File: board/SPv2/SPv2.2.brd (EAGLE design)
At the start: 60 x 22.9 mm, 35 parts, among them IC1 S34ML0XG1, IC2 F5508, IC4 74LS14D, Q1 12MHz

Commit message: * some updates for v2.2 of the board (reducing components) * cleaning up error code * verifying R codes do work
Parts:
- moved D1 2.25 mm to (13.3, 6.35)
- moved R21 0.32 mm to (19.5, 10.8)
- flipped SJ1 to the bottom, turned to 0 degrees
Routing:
- net GND: track 169.0 -> 164.6 mm, vias 9 -> 8
- net VBUS: track 87.8 -> 84.5 mm
- net N$4: track 2.86 -> 0.02 mm
- net PUR_A: track 15.0 -> 12.5 mm
- net N$33: track 4.52 -> 6.59 mm

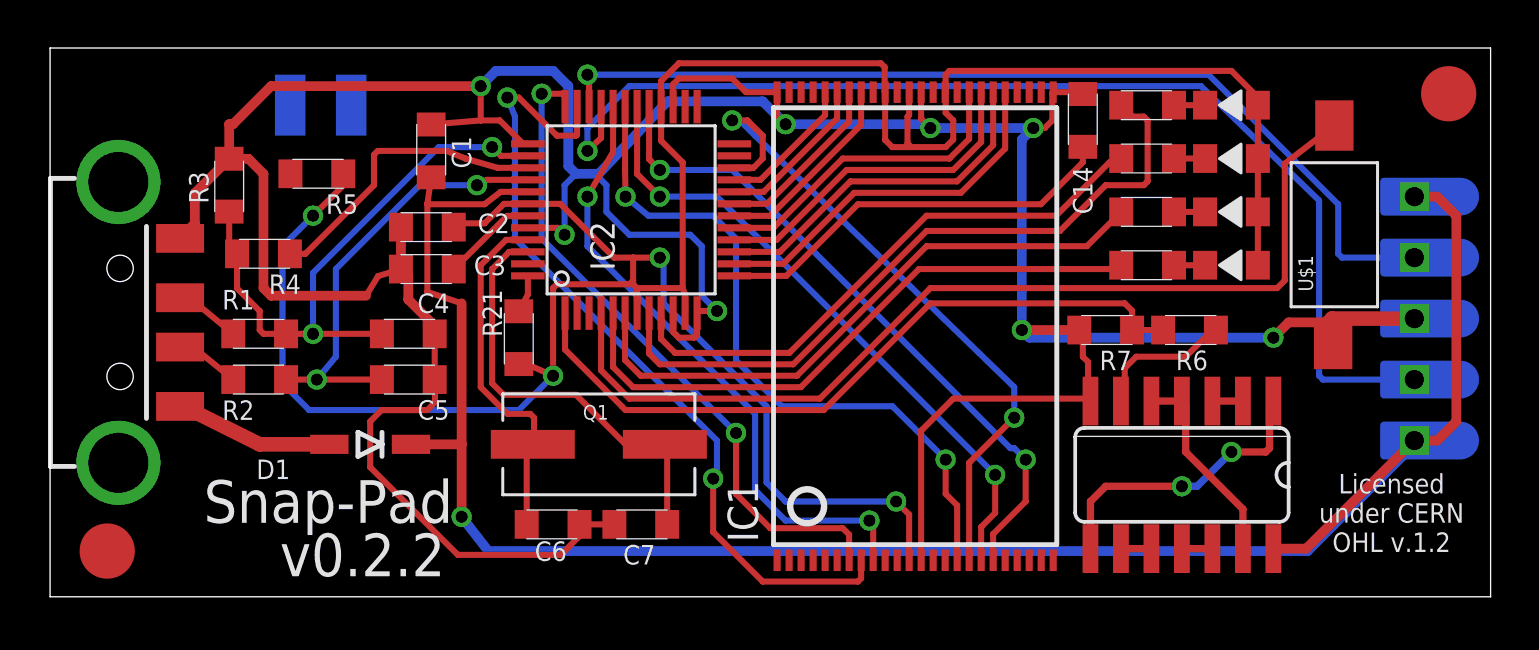
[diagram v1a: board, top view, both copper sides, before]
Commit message: new switch smaller 74ls14 jumper header instead of solder jumper board layout in progress
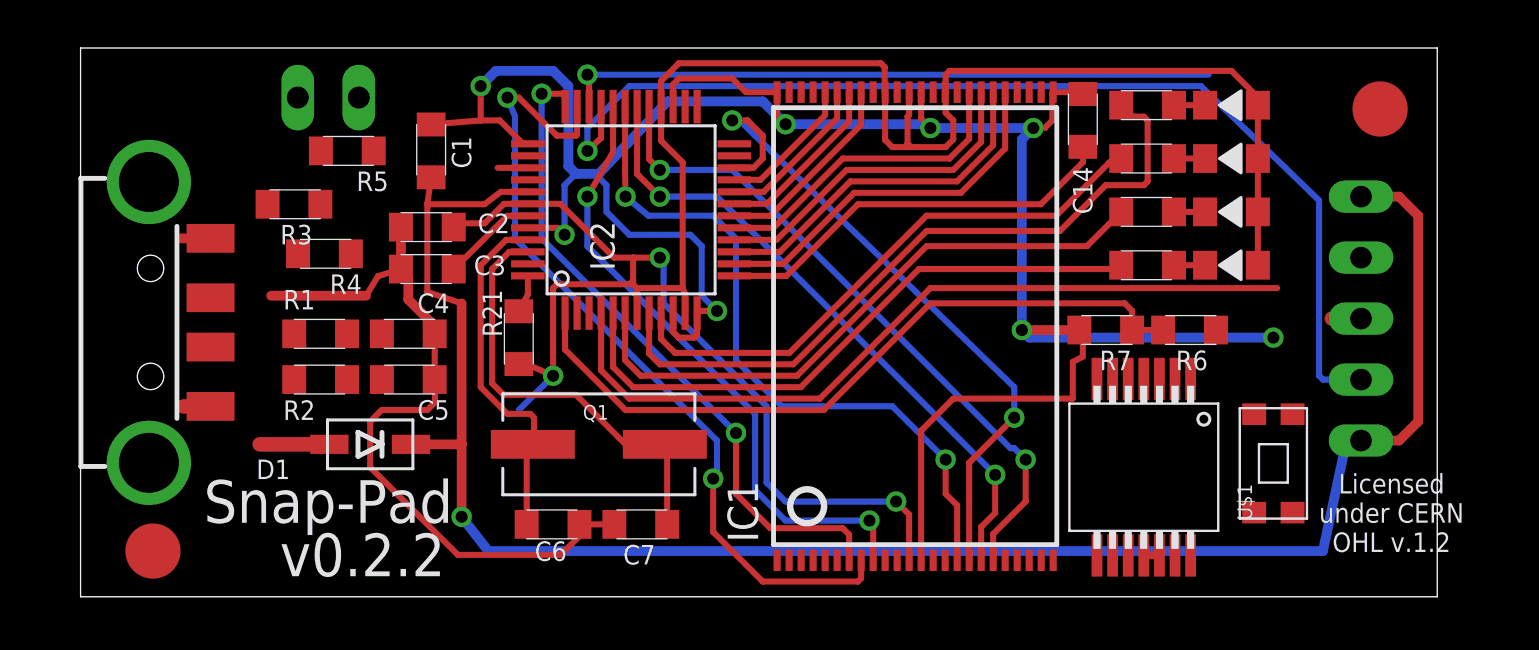
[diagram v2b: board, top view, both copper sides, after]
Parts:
- IC4: value 74LS14D -> 74LS14DB; device 74xx-us:SO14 -> 74xx-db-us:SSOP14
- SJ1: device jumper:SJW -> jumper:JP1
- U$1: value FSMSM -> KMR-2; device Passives:FSMSM -> Passives:KMR-2-SWITCH
- moved U$1 9.86 mm to (51.0, 5.56)
- moved U$12 2.93 mm to (55.4, 20.3)
- moved R3 2.81 mm to (10.2, 16.4), turned to 180 degrees
- moved R1 2.54 mm to (11.3, 11.0)
- moved R2 2.54 mm to (11.3, 9.05)
- moved R4 2.54 mm to (11.4, 14.3)
- moved U$2 2.22 mm to (58.4, 11.6)
- moved U$3 1.90 mm to (4.29, 1.91)
- moved IC4 1.62 mm to (45.6, 5.40)
- moved R5 1.59 mm to (12.4, 18.6)
- moved JP1 1.27 mm to (3.02, 11.4)
- moved SJ1 0.45 mm to (11.6, 20.8), turned to 270 degrees
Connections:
- net GND: now also U$1.PA1, U$1.PA2; no longer U$1.P$1
- net SW_A: now also U$1.PB1, U$1.PB2; no longer U$1.P$2
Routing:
- net GND: track 164.6 -> 134.9 mm
- net D+_A: track 24.8 -> 0.00 mm, vias 2 -> 0
- net +3V3_A: track 116.2 -> 96.1 mm, vias 4 -> 3
- net D-_A: track 18.4 -> 0.00 mm, vias 2 -> 0
- net N$7: track 12.4 -> 0.00 mm, vias 2 -> 0
- net RX_A: track 40.2 -> 28.2 mm
- net PUR_A: track 12.5 -> 1.26 mm
- net N$9: track 8.47 -> 0.00 mm
- net SW_A: track 40.9 -> 32.9 mm
- net VBUS: track 84.5 -> 77.4 mm
- net N$10: track 5.89 -> 0.00 mm
- net N$33: track 6.59 -> 4.03 mm
- net TX_A: track 47.5 -> 45.3 mm
- net N$2: track 2.71 -> 0.75 mm
- net N$1: track 2.75 -> 0.85 mm
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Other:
- board size 60 x 22.9 mm -> 56.5 x 22.9 mm

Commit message: rerouting in progress
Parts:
- added TP1, TP2, TP3, TP4: TPTP13R, testpad:TP13R
- moved C1 1.00 mm to (15.6, 19.5)
- moved R1 0.95 mm to (10.3, 11.0)
- moved R2 0.95 mm to (10.3, 9.05)
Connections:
- net GND: now also TP4.TP
- net N$1: now also TP1.TP
- net N$2: now also TP2.TP
- net N$33: now also TP3.TP
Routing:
- net D+_A: track 0.00 -> 28.6 mm, vias 0 -> 3
- net D-_A: track 0.00 -> 18.3 mm, vias 0 -> 2
- net GND: track 134.9 -> 146.9 mm, vias 8 -> 9
- net N$2: track 0.75 -> 10.3 mm, vias 0 -> 1
- net N$1: track 0.85 -> 9.62 mm, vias 0 -> 1
- net N$33: track 4.03 -> 10.5 mm, vias 0 -> 1
- net VBUS: track 77.4 -> 78.4 mm

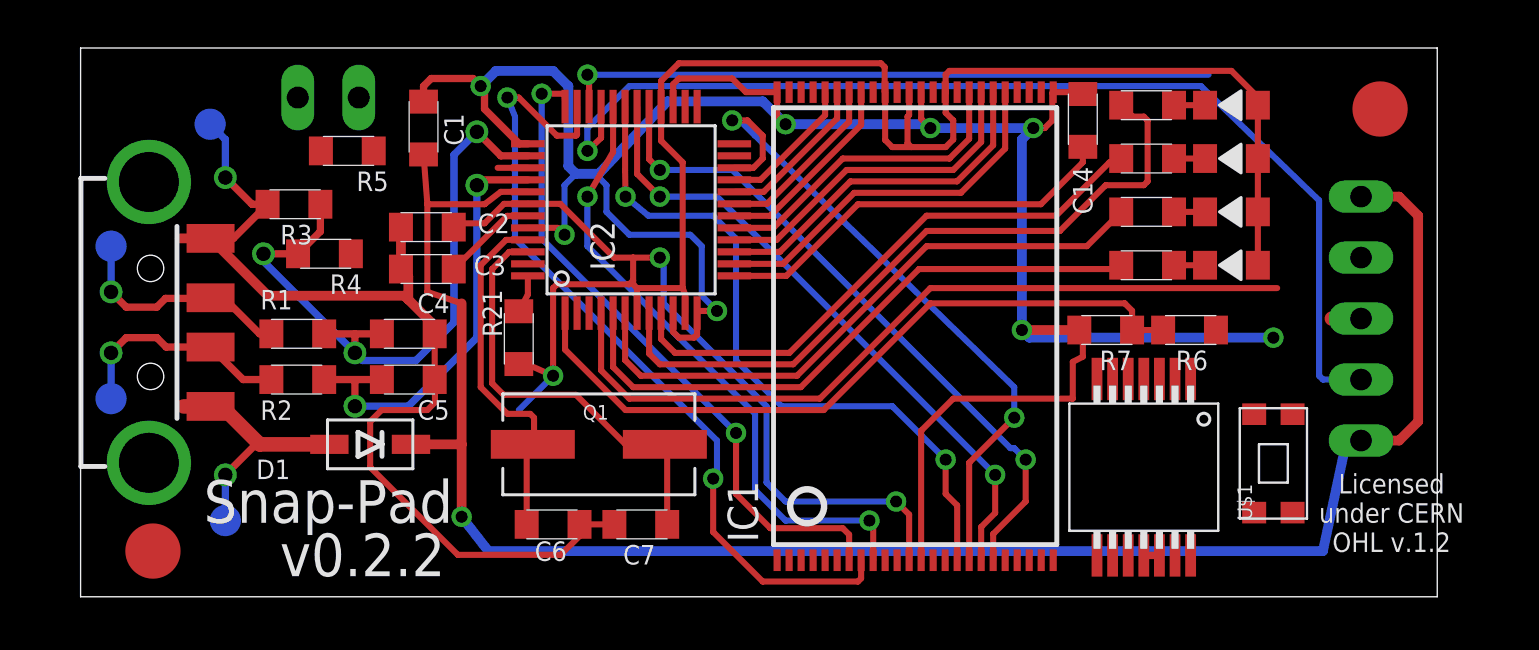
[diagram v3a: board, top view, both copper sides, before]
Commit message: yet more routing; just the ring oscillator noodling to finish
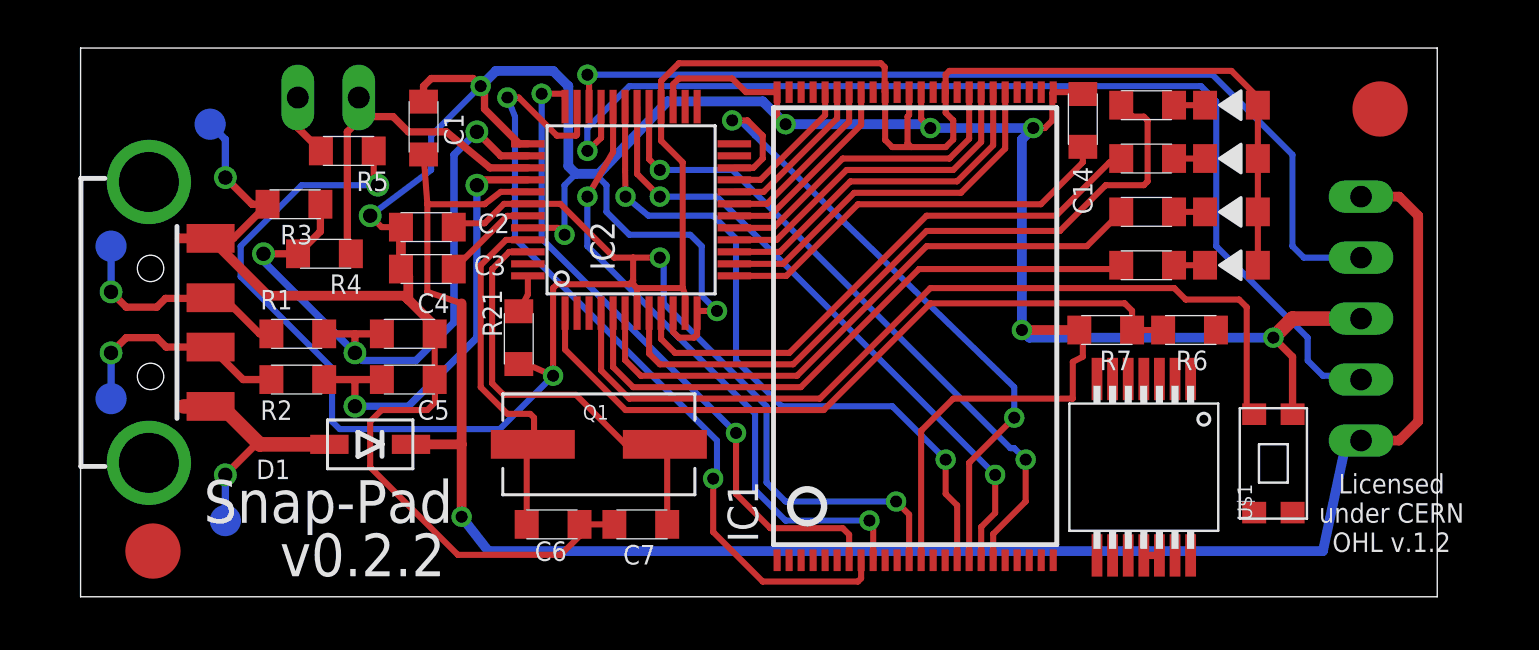
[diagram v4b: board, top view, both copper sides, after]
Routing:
- net +3V3_A: track 96.1 -> 121.5 mm, vias 3 -> 4
- net GND: track 146.9 -> 162.2 mm, vias 9 -> 10
- net PUR_A: track 1.26 -> 14.6 mm
- net RX_A: track 28.2 -> 39.0 mm
- net SW_A: track 32.9 -> 36.6 mm
- net N$4: track 0.00 -> 2.62 mm
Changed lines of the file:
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@@
 <wire x1="43.02125" y1="10.965" x2="42.87375" y2="11.1125" width="0.254" layer="1"/>
 <contactref element="U$2" pad="P$3"/>
-<wire x1="54.61" y1="11.58875" x2="53.395" y2="11.58875" width="0.6096" layer="1"/>
 <via x="50.95875" y="10.795" extent="1-16" drill="0.5"/>
 <wire x1="50.95875" y1="10.795" x2="40.79875" y2="10.795" width="0.4064" layer="16"/>
@@
 <wire x1="15.875" y1="21.59" x2="17.62125" y2="21.59" width="0.3048" layer="1"/>
 <wire x1="17.62125" y1="21.59" x2="17.93875" y2="21.2725" width="0.3048" layer="1"/>
-<wire x1="50.95875" y1="10.795" x2="53.395" y2="11.58875" width="0" layer="19" extent="1-1"/>
-<wire x1="43.61125" y1="9.0725" x2="43.02125" y2="10.00125" width="0" layer="19" extent="1-1"/>
-<wire x1="51.75875" y1="7.60625" x2="50.95875" y2="10.795" width="0" layer="19" extent="1-1"/>
-<wire x1="14.61625" y1="15.39875" x2="19.90373125" y2="15.368765625" width="0" layer="19" extent="1-1"/>
 <wire x1="14.76375" y1="12.54125" x2="14.9225" y2="12.3825" width="0.4064" layer="1"/>
 <wire x1="9.075" y1="12.54125" x2="6.68625" y2="14.93" width="0.4064" layer="1"/>
@@
 <wire x1="7.3025" y1="17.4625" x2="7.3025" y2="19.05" width="0.3048" layer="16"/>
 <wire x1="7.3025" y1="19.05" x2="6.6675" y2="19.685" width="0.3048" layer="16"/>
+<wire x1="14.61625" y1="15.39875" x2="13.81125" y2="15.39875" width="0.254" layer="1"/>
+<wire x1="13.81125" y1="15.39875" x2="13.335" y2="15.875" width="0.254" layer="1"/>
+<via x="13.335" y="15.875" extent="1-16" drill="0.6"/>
+<wire x1="13.335" y1="15.875" x2="15.875" y2="17.78" width="0.254" layer="16"/>
+<wire x1="15.875" y1="17.78" x2="15.875" y2="19.20875" width="0.254" layer="16"/>
+<wire x1="15.875" y1="19.20875" x2="17.93875" y2="21.2725" width="0.254" layer="16"/>
+<wire x1="54.61" y1="11.58875" x2="51.7525" y2="11.58875" width="0.6096" layer="1"/>
+<wire x1="51.7525" y1="11.58875" x2="50.95875" y2="10.795" width="0.6096" layer="1"/>
+<wire x1="51.75875" y1="7.60625" x2="51.75875" y2="9.995" width="0.3048" layer="1"/>
+<wire x1="51.75875" y1="9.995" x2="50.95875" y2="10.795" width="0.3048" layer="1"/>
+<wire x1="43.02125" y1="10.00125" x2="43.61125" y2="9.0725" width="0" layer="19" extent="1-1"/>
 </signal>
 <signal name="+3V3_A">
@@
 <wire x1="21.11375" y1="13.0175" x2="24.13" y2="13.0175" width="0.254" layer="1"/>
 <wire x1="24.13" y1="13.0175" x2="24.28875" y2="13.17625" width="0.254" layer="1"/>
-<wire x1="19.52625" y1="7.77875" x2="20.955" y2="9.2075" width="0.254" layer="16"/>
+<wire x1="18.7325" y1="6.985" x2="20.955" y2="9.2075" width="0.254" layer="16"/>
 <via x="20.955" y="9.2075" extent="1-16" drill="0.5"/>
 <wire x1="19.90373125" y1="16.368765625" x2="18.908765625" y2="16.368765625" width="0.254" layer="1"/>
@@
 <wire x1="18.0975" y1="15.5575" x2="16.975" y2="15.5575" width="0.254" layer="1"/>
 <wire x1="16.975" y1="15.5575" x2="16.81625" y2="15.39875" width="0.254" layer="1"/>
-<wire x1="16.81625" y1="15.39875" x2="13.4825" y2="18.57375" width="0" layer="19" extent="1-1"/>
+<wire x1="13.4825" y1="18.57375" x2="13.4825" y2="17.315" width="0.254" layer="1"/>
+<wire x1="13.4825" y1="17.315" x2="13.6525" y2="17.145" width="0.254" layer="1"/>
+<via x="13.6525" y="17.145" extent="1-16" drill="0.6"/>
+<wire x1="13.6525" y1="17.145" x2="10.4775" y2="17.145" width="0.254" layer="16"/>
+<wire x1="10.4775" y1="17.145" x2="7.9375" y2="14.605" width="0.254" layer="16"/>
+<wire x1="7.9375" y1="14.605" x2="7.9375" y2="13.335" width="0.254" layer="16"/>
+<wire x1="7.9375" y1="13.335" x2="11.7475" y2="9.525" width="0.254" layer="16"/>
+<wire x1="11.7475" y1="9.525" x2="11.7475" y2="7.3025" width="0.254" layer="16"/>
+<wire x1="11.7475" y1="7.3025" x2="12.065" y2="6.985" width="0.254" layer="16"/>
+<wire x1="12.065" y1="6.985" x2="18.7325" y2="6.985" width="0.254" layer="16"/>
 </signal>
 <signal name="VBUS">
@@
 <contactref element="SJ1" pad="1"/>
 <contactref element="R4" pad="P$2"/>
-<wire x1="19.90373125" y1="17.868765625" x2="18.643734375" y2="17.868765625" width="0.254" layer="1"/>
-<wire x1="12.85875" y1="20.79625" x2="18.643734375" y2="17.868765625" width="0" layer="19" extent="1-1"/>
-<wire x1="12.53" y1="14.2875" x2="12.85875" y2="20.79625" width="0" layer="19" extent="1-1"/>
+<wire x1="12.85875" y1="20.79625" x2="12.85875" y2="20.0025" width="0.3048" layer="1"/>
+<wire x1="12.85875" y1="20.0025" x2="12.85875" y2="19.84375" width="0.3048" layer="1"/>
+<wire x1="12.85875" y1="19.84375" x2="12.3825" y2="19.3675" width="0.3048" layer="1"/>
+<wire x1="12.3825" y1="19.3675" x2="12.3825" y2="14.435" width="0.3048" layer="1"/>
+<wire x1="12.3825" y1="14.435" x2="12.53" y2="14.2875" width="0.3048" layer="1"/>
+<wire x1="19.90373125" y1="17.868765625" x2="18.326234375" y2="17.868765625" width="0.3048" layer="1"/>
+<wire x1="18.326234375" y1="17.868765625" x2="16.51" y2="19.3675" width="0.3048" layer="1"/>
+<wire x1="16.51" y1="19.3675" x2="14.9225" y2="19.3675" width="0.3048" layer="1"/>
+<wire x1="14.9225" y1="19.3675" x2="14.2875" y2="20.0025" width="0.3048" layer="1"/>
+<wire x1="14.2875" y1="20.0025" x2="12.85875" y2="20.0025" width="0.3048" layer="1"/>
 </signal>
 <signal name="TDO_A">
@@
 <contactref element="R5" pad="P$1"/>
 <contactref element="SJ1" pad="2"/>
-<wire x1="11.2825" y1="18.57375" x2="10.31875" y2="20.79625" width="0" layer="19" extent="1-1"/>
+<wire x1="10.31875" y1="20.79625" x2="10.31875" y2="19.5375" width="0.3048" layer="1"/>
+<wire x1="10.31875" y1="19.5375" x2="11.2825" y2="18.57375" width="0.3048" layer="1"/>
 </signal>
 <signal name="SW_A">
@@
 <wire x1="22.95373125" y1="9.43126875" x2="24.13" y2="8.255" width="0.254" layer="1"/>
 <wire x1="24.13" y1="8.255" x2="32.0675" y2="8.255" width="0.254" layer="1"/>
-<wire x1="51.1175" y1="12.85875" x2="36.67125" y2="12.85875" width="0.254" layer="1"/>
 <wire x1="36.67125" y1="12.85875" x2="32.0675" y2="8.255" width="0.254" layer="1"/>
 <contactref element="U$1" pad="PB2" route="any" routetag="G$1.B"/>
-<wire x1="51.1175" y1="12.85875" x2="50.15875" y2="7.60625" width="0" layer="19" extent="1-1"/>
+<wire x1="36.67125" y1="12.85875" x2="46.83125" y2="12.85875" width="0.254" layer="1"/>
+<wire x1="46.83125" y1="12.85875" x2="47.3075" y2="12.3825" width="0.254" layer="1"/>
+<wire x1="47.3075" y1="12.3825" x2="49.53" y2="12.3825" width="0.254" layer="1"/>
+<wire x1="49.53" y1="12.3825" x2="49.8475" y2="12.065" width="0.254" layer="1"/>
+<wire x1="49.8475" y1="12.065" x2="49.8475" y2="7.9175" width="0.254" layer="1"/>
+<wire x1="49.8475" y1="7.9175" x2="50.15875" y2="7.60625" width="0.254" layer="1"/>
 </signal>
 <signal name="N$33">
@@
 <wire x1="22.45373125" y1="21.36126875" x2="22.38375" y2="21.74875" width="0.254" layer="1"/>
 <via x="22.38375" y="21.74875" extent="1-16" drill="0.5"/>
-<wire x1="22.38375" y1="21.74875" x2="48.26" y2="21.74875" width="0.254" layer="16"/>
-<wire x1="53.6575" y1="14.2875" x2="53.81625" y2="14.12875" width="0.254" layer="16"/>
+<wire x1="22.38375" y1="21.74875" x2="48.41875" y2="21.74875" width="0.254" layer="16"/>
 <contactref element="U$2" pad="P$4"/>
-<wire x1="54.61" y1="14.12875" x2="53.81625" y2="14.12875" width="0.254" layer="16"/>
-<wire x1="48.26" y1="21.74875" x2="53.6575" y2="14.2875" width="0" layer="19" extent="16-16"/>
+<wire x1="48.41875" y1="21.74875" x2="51.7525" y2="18.415" width="0.254" layer="16"/>
+<wire x1="51.7525" y1="18.415" x2="51.7525" y2="14.605" width="0.254" layer="16"/>
+<wire x1="51.7525" y1="14.605" x2="52.22875" y2="14.12875" width="0.254" layer="16"/>
+<wire x1="52.22875" y1="14.12875" x2="54.61" y2="14.12875" width="0.254" layer="16"/>
 </signal>
 <signal name="TX_A">
@@
 <wire x1="22.38375" y1="19.52625" x2="24.13" y2="21.2725" width="0.254" layer="16"/>
 <wire x1="24.13" y1="21.2725" x2="47.9425" y2="21.2725" width="0.254" layer="16"/>
-<wire x1="47.9425" y1="21.2725" x2="52.86375" y2="16.51" width="0.254" layer="16"/>
-<wire x1="52.86375" y1="16.51" x2="52.86375" y2="9.2075" width="0.254" layer="16"/>
 <contactref element="U$2" pad="P$2"/>
-<wire x1="54.61" y1="9.04875" x2="53.0225" y2="9.04875" width="0.254" layer="16"/>
-<wire x1="53.0225" y1="9.04875" x2="52.86375" y2="9.2075" width="0.254" layer="16"/>
+<wire x1="47.9425" y1="21.2725" x2="48.5775" y2="20.6375" width="0.254" layer="16"/>
+<wire x1="48.5775" y1="20.6375" x2="48.5775" y2="14.605" width="0.254" layer="16"/>
+<wire x1="48.5775" y1="14.605" x2="52.3875" y2="10.795" width="0.254" layer="16"/>
+<wire x1="52.3875" y1="10.795" x2="52.3875" y2="9.8425" width="0.254" layer="16"/>
+<wire x1="52.3875" y1="9.8425" x2="53.0225" y2="9.2075" width="0.254" layer="16"/>
+<wire x1="53.0225" y1="9.2075" x2="54.45125" y2="9.2075" width="0.254" layer="16"/>
+<wire x1="54.45125" y1="9.2075" x2="54.61" y2="9.04875" width="0.254" layer="16"/>
 </signal>
 <signal name="N$5">
